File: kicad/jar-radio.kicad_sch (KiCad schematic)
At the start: 58 parts, among them J1 USB-C 5V, J2 18650 holder, J3 ANT wire, J4 SPK wires, Q1 AO3401A, SW1 POWER, U1 Si4825-A10, U2 NS8002, U3 TP4056, U4 XC6206P332MR, U5 XC61CN2702MR, Y1 32.768kHz

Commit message: Rev F.8: no connectors, holder slot 180 deg from speaker, fix VBUS-GND stub collision in schematic generator
Co-Authored-By: Claude Opus 5.5 <noreply@anthropic.com>
Claude-Session: https://claude.ai/code/session_01UChZ4MGw6SzykNSB399iC4
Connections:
- net GND: no longer C15.1, D1.2 (A), J1.2 (VBUS), J1.5 (VBUS), Q1.1 (G), R14.1, R15.1, R16.1, U3.4 (VCC), U3.8 (CE)
- new net VBUS: C15.1, D1.2 (A), J1.2 (VBUS), J1.5 (VBUS), Q1.1 (G), R14.1, R15.1, R16.1, U3.4 (VCC), U3.8 (CE)
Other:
- note added: "ANTENNA - wire soldered into J3 (2 zip-tie holes) or telescopic whip on ANT1; AN738 whip network"
- note added: "AUDIO - volume pot RV1, NS8002 class AB BTL, Av = 2*R8/R7 = 20"
- note added: "POWER - USB-C in, TP4056 charger, AN1149 load sharing, slide switch SW1, 3.3 V LDO"
- note removed: "ANTENNA - wire on J3 (XH) or telescopic whip on ANT1; AN738 whip network"
- note removed: "AUDIO - volume pot (switch = power), NS8002 class AB BTL, Av = 2*R8/R7 = 20"
- note removed: "POWER - USB-C in, TP4056 charger (400 mA), AN1149 load sharing, pot switch, 3.3 V LDO"

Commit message: Rev F.9: XB8089D + PTC protection, switched pot (CTR R097NS) replaces slide switch, SP3021 ESD, 500 mA charge, Basic green LED, local JLC parts DB + BOM checker
Co-Authored-By: Claude Opus 5.5 <noreply@anthropic.com>
Claude-Session: https://claude.ai/code/session_01UChZ4MGw6SzykNSB399iC4
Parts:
- removed RV1: 50k audio, jar-radio:Potentiometer_Bourns_PTV09A-4_RearMount, symbol jar-radio:Pot3
- removed SW1: POWER, Button_Switch_SMD:SW_SPDT_PCM12, symbol jar-radio:SW_SPDT
- added C22: 100nF, Capacitor_SMD:C_0603_1608Metric, symbol jar-radio:C
- added F1: PTC 1.1A, Fuse:Fuse_1206_3216Metric, symbol jar-radio:R
- added R18: 1k, Resistor_SMD:R_0603_1608Metric, symbol jar-radio:R
- added RV1: 50k B + SW, jar-radio:Potentiometer_RV097NS_Switch_Vertical_PROVISIONAL, symbol jar-radio:Pot_Switch
- added U6: XB8089D, Package_SO:SOIC-8-1EP_3.9x4.9mm_P1.27mm_EP2.41x3.3mm, symbol jar-radio:XB8089D
- D3: footprint LED_SMD:LED_0603_1608Metric -> LED_SMD:LED_0805_2012Metric; LCSC C72043 -> C2297; MPN 19-217/GHC-YR1S2/3T -> KT-0805G
- D4: value ESD <=1pF -> ESD 0.5pF; LCSC C5139344 -> C126839; MPN PESD5V0F1BL -> SP3021-01ETG
- R13: value 3.0k -> 2.4k; LCSC C4211 -> C22940; MPN 0603WAF3001T5E -> 0603WAF2401T5E
- R15: value 2.2k -> 1k; LCSC C4190 -> C21190; MPN 0603WAF2201T5E -> 0603WAF1001T5E
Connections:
- net GND: now also RV1.1 (CCW), RV1.MP (MOUNT), U6.1 (VM), U6.2 (VM), U6.3 (VM), U6.4 (VM); no longer J2.2
- net VBAT: now also F1.2; no longer J2.1
- net VOL_TOP: now also RV1.3 (CW)
- net VOL_WIPER: now also RV1.2 (WIPER)
- net VSW: now also RV1.S2 (SW_B)
- net VSYS: now also RV1.S1 (SW_A)
- new net BAT_N: C22.2, J2.2, U6.5 (GND), U6.7 (GND), U6.8 (GND), U6.9 (EP)
- new net BAT_P: F1.1, J2.1, R18.1
- new net XB_VDD: C22.1, R18.2, U6.6 (VDD)
- no-connect marks 3 -> 2

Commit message: Rev F.10: USB-C C30167335 footprint, reset/ESD/PTC/NTC kept as DNP upgrade spots, pot datasheets show right-angle
Co-Authored-By: Claude Opus 5.5 <noreply@anthropic.com>
Claude-Session: https://claude.ai/code/session_01UChZ4MGw6SzykNSB399iC4
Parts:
- added R20: 5.1k (DNP), Resistor_SMD:R_0603_1608Metric, symbol jar-radio:R
- added R21: 0R, Resistor_SMD:R_0603_1608Metric, symbol jar-radio:R
- added RT1: NTC 10k B3950 (DNP), Resistor_SMD:R_0603_1608Metric, symbol jar-radio:R
- D4, U5: Note (none) -> DNP; now not fitted
- F1: value PTC 1.1A -> 0R (PTC spot); LCSC C269119 -> C17888; MPN SMD1206B110TFT -> 1206W4F0000T5E
- J1: footprint jar-radio:USB_C_Receptacle_ShouHan_TYPE-C-6PLTH6.8-DJ_Vertical -> jar-radio:USB_C_Receptacle_ShouHan_TYPE-C-6P-LTH6.8-108_Vertical; LCSC C5156600 -> C30167335; MPN TYPE-C 6PLTH6.8-DJ -> TYPE-C 6P LTH6.8 108
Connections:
- net GND: now also R21.2, RT1.2; no longer U3.1 (TEMP)
- net VBUS: now also R20.1
- new net TEMP: R20.2, R21.1, RT1.1, U3.1 (TEMP)

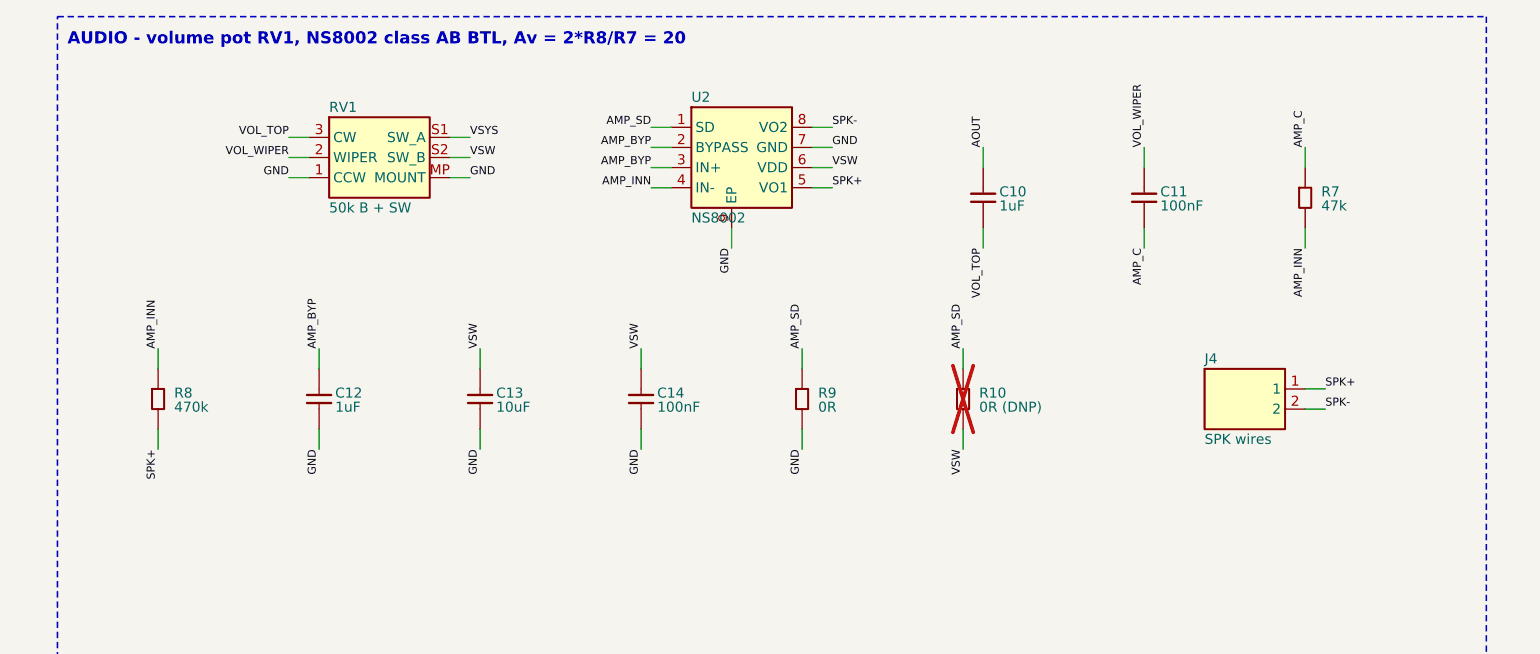
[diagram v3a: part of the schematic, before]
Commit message: Rev F.12: RV1 = CTR R09512NS rear-mount switched pot (C18213422), footprint from drawing, R22 4.7k + R8 680k for 10k pot
Co-Authored-By: Claude Opus 5.5 <noreply@anthropic.com>
Claude-Session: https://claude.ai/code/session_01UChZ4MGw6SzykNSB399iC4
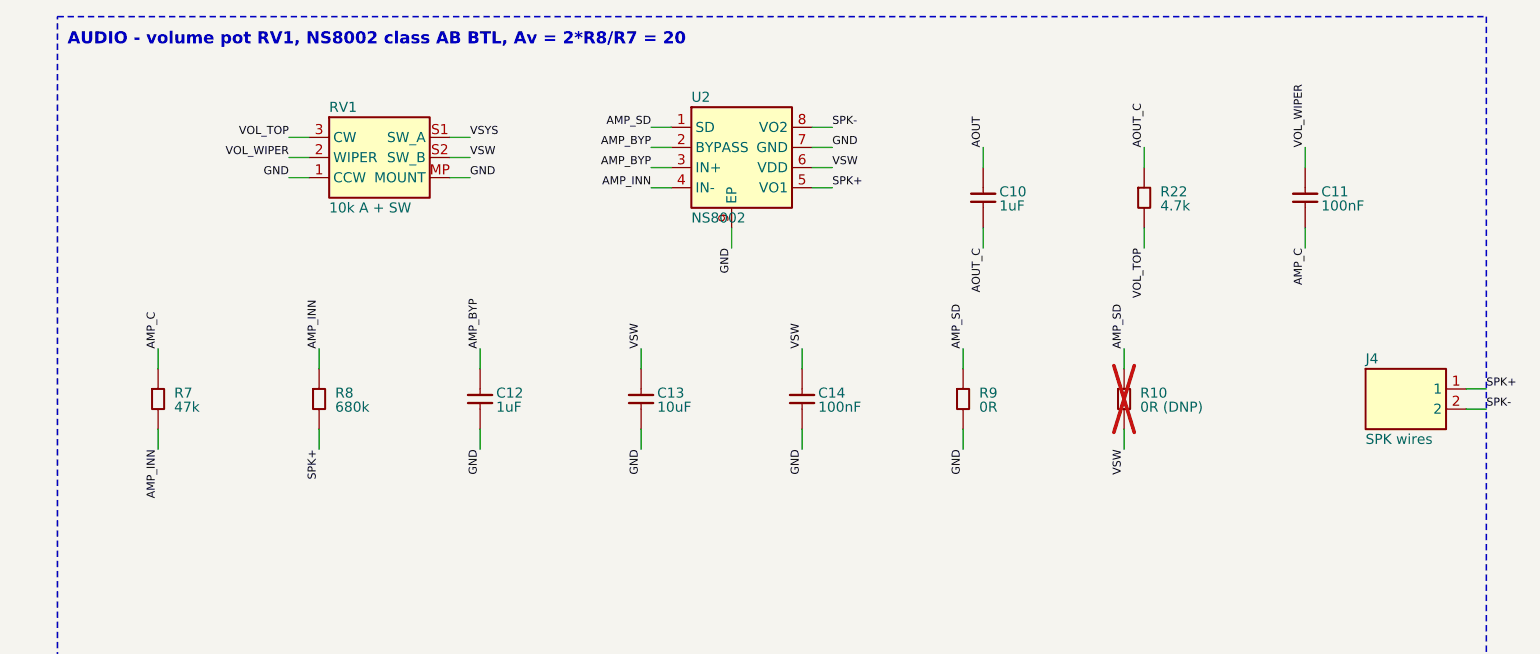
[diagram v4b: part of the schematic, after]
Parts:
- added R22: 4.7k, Resistor_SMD:R_0603_1608Metric, symbol jar-radio:R
- R8: value 470k -> 680k; LCSC C23178 -> C25822; MPN 0603WAF4703T5E -> 0603WAF6803T5E
- RV1: value 50k B + SW -> 10k A + SW; footprint jar-radio:Potentiometer_RV097NS_Switch_Vertical_PROVISIONAL -> jar-radio:Potentiometer_CTR_R09512NS_RearMount_Switch; LCSC C18213431 -> C18213422; MPN R09760NS-FB15A7.0-B503-0P7 -> R09512NS-FB15S7.0-A103-00G
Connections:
- net VOL_TOP: now also R22.2; no longer C10.2
- new net AOUT_C: C10.2, R22.1

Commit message: Cost-down: station resistors 82k/11k 1% (fee-free), C7/C21 22uF 0603, C18 10uF 0603; re-routed (0 unconnected, 0 clearance), re-exported, plan updated
Co-Authored-By: Claude Opus 5.5 <noreply@anthropic.com>
Claude-Session: https://claude.ai/code/session_01UChZ4MGw6SzykNSB399iC4
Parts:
- C18: value 22uF -> 10uF; footprint Capacitor_SMD:C_0805_2012Metric -> Capacitor_SMD:C_0603_1608Metric; LCSC C45783 -> C19702; MPN CL21A226MAQNNNE -> CL10A106KP8NNNC
- C21, C7: footprint Capacitor_SMD:C_0805_2012Metric -> Capacitor_SMD:C_0603_1608Metric; LCSC C45783 -> C59461; MPN CL21A226MAQNNNE -> CL10A226MQ8NRNC
- R2: value 86.6k 0.1% -> 82k; LCSC C861580 -> C23254; MPN RT0603BRD0786K6L -> 0603WAF8202T5E
- R3: value 11.7k 0.1% -> 11k; LCSC C4553285 -> C25950; MPN TNPW060311K7BEEA -> 0603WAF1102T5E
